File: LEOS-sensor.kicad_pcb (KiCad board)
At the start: 2 copper layers, 100 x 100 mm, 25 parts, among them J1 MicroFit_1x4, J2 MicroFit_1x4, J3 Conn_01x04_Pin, J4 Conn_01x06_Pin, J5 Conn_01x06_Pin, J6 Conn_01x05_Pin, J7 Conn_01x05_Pin, J8 Conn_01x04_Pin, U1 MCP2562FD, U2 MCP2518FD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

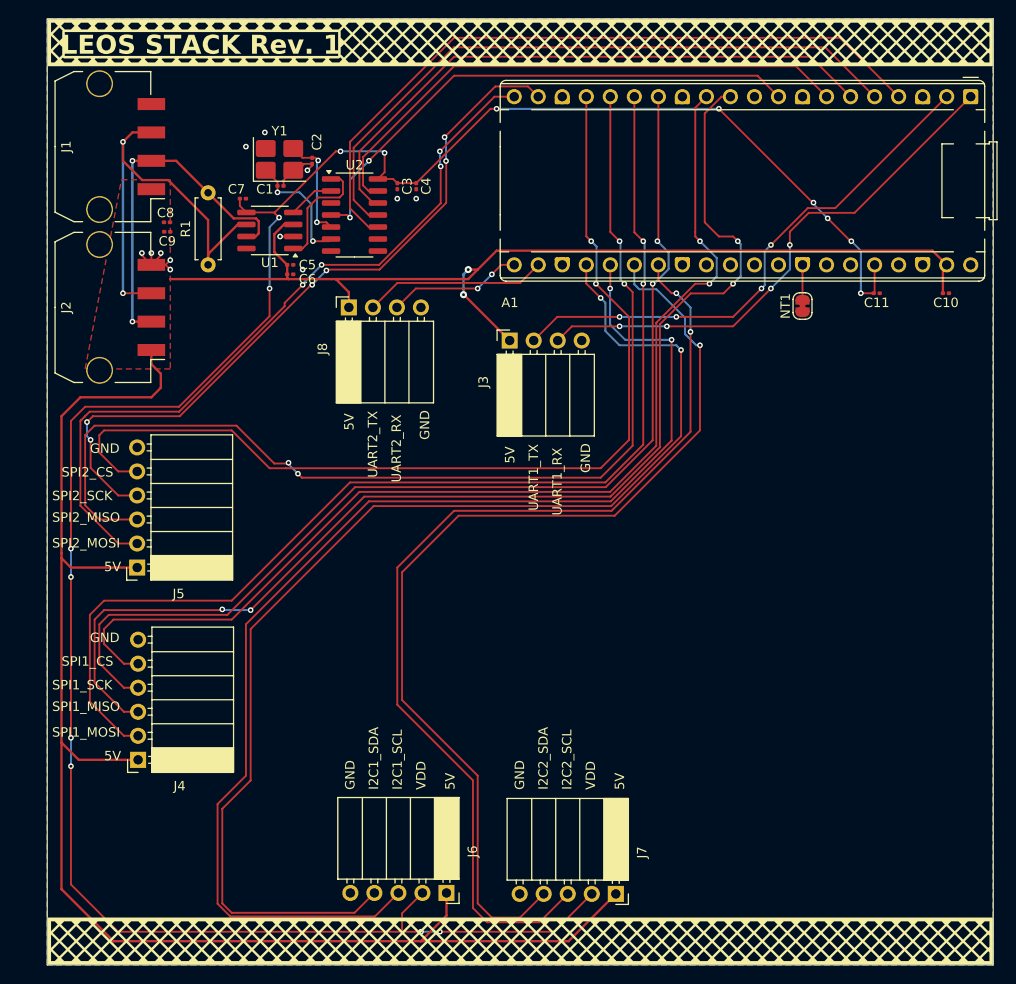
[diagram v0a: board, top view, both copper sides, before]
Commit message: Converted schematic to Socket schematics and routed all headers
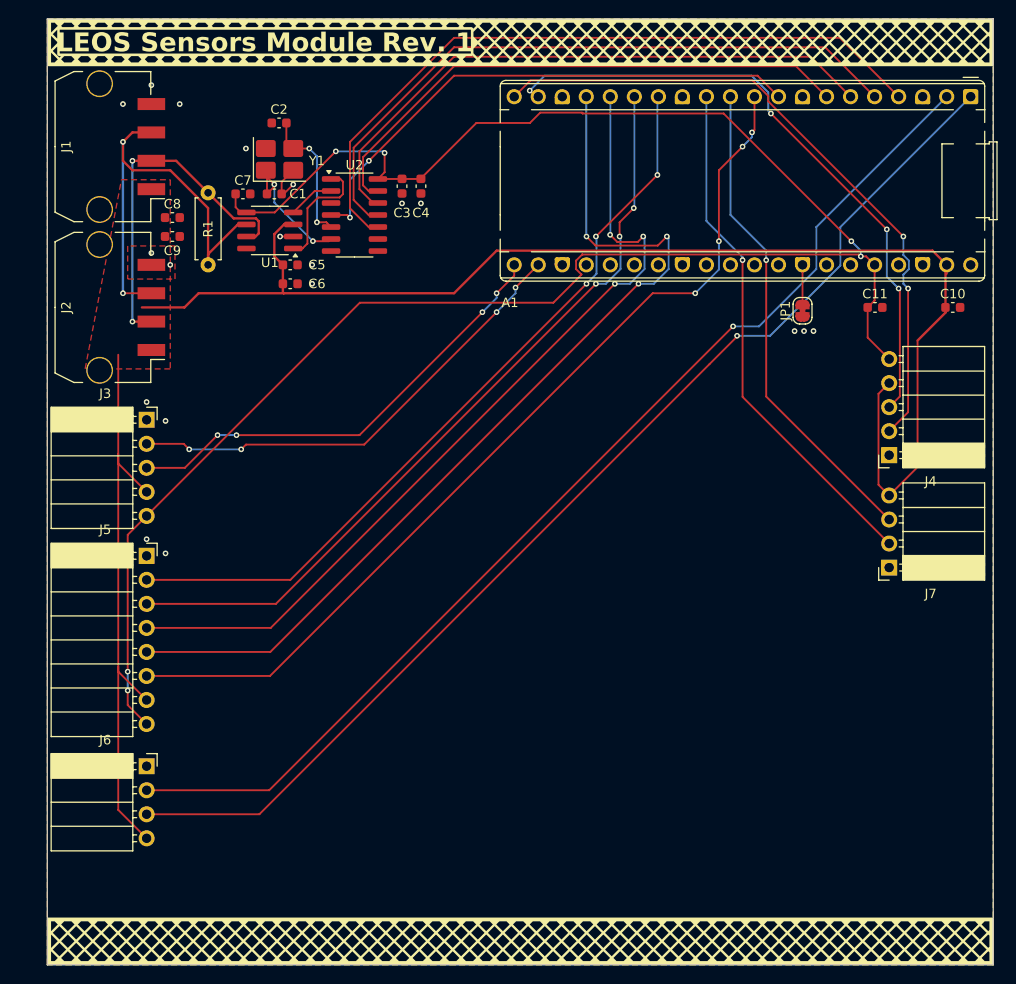
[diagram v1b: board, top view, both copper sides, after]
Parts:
- removed J8: Conn_01x04_Pin, Connector_PinSocket_2.54mm:PinSocket_1x04_P2.54mm_Horizontal
- removed NT1: NetTie_2, Jumper:SolderJumper-2_P1.3mm_Bridged_RoundedPad1.0x1.5mm
- added JP1: AGND Tie, Jumper:SolderJumper-2_P1.3mm_Bridged_RoundedPad1.0x1.5mm, F.Cu at (179.8, 80.8)
- C1, C10, C11, C2, C3, C4, C5, C6, C7, C8, C9: footprint Capacitor_SMD:C_0201_0603Metric -> Capacitor_SMD:C_0603_1608Metric
- J3: value Conn_01x04_Pin -> I2C 0; footprint Connector_PinSocket_2.54mm:PinSocket_1x04_P2.54mm_Horizontal -> Connector_PinSocket_2.54mm:PinSocket_1x05_P2.54mm_Horizontal
- J4: value Conn_01x06_Pin -> I2C 1; footprint Connector_PinSocket_2.54mm:PinSocket_1x06_P2.54mm_Horizontal -> Connector_PinSocket_2.54mm:PinSocket_1x05_P2.54mm_Horizontal
- J5: value Conn_01x06_Pin -> SPI 1; footprint Connector_PinSocket_2.54mm:PinSocket_1x06_P2.54mm_Horizontal -> Connector_PinSocket_2.54mm:PinSocket_1x08_P2.54mm_Horizontal
- J6: value Conn_01x05_Pin -> UART 0; footprint Connector_PinSocket_2.54mm:PinSocket_1x05_P2.54mm_Horizontal -> Connector_PinSocket_2.54mm:PinSocket_1x04_P2.54mm_Horizontal
- J7: value Conn_01x05_Pin -> UART 1; footprint Connector_PinSocket_2.54mm:PinSocket_1x05_P2.54mm_Horizontal -> Connector_PinSocket_2.54mm:PinSocket_1x04_P2.54mm_Horizontal
- moved J4 85.7 mm to (189.0, 96.1)
- moved J7 45.0 mm to (189.0, 108.0), turned to 180 degrees
- moved J3 39.3 mm to (110.5, 92.4), turned to 0 degrees
- moved J6 34.4 mm to (110.5, 129.0), turned to 0 degrees
- moved C2 5.32 mm to (124.5, 61.0), turned to 0 degrees
- moved C10 1.67 mm to (195.7, 80.5)
- moved J5 1.59 mm to (110.5, 106.8), turned to 0 degrees
- moved C11 1.51 mm to (187.5, 80.5)
- moved C1 1.07 mm to (124.0, 68.5)
- moved C6 1.00 mm to (125.7, 78.0)
- moved C8 0.76 mm to (113.2, 71.0)
- moved C9 0.74 mm to (113.2, 73.0)
- moved C3 0.50 mm to (137.5, 67.7)
- moved C4 0.50 mm to (139.5, 67.7)
- moved C7 0.50 mm to (120.7, 68.5)
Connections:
- A1 pad 1: UART1_RX -> UART0_TX
- A1 pad 11: SPI1_MISO -> UART1_TX
- A1 pad 12: SPI1_CS -> UART1_RX
- A1 pad 16: SPI2_MISO -> SPI1_MISO
- A1 pad 17: SPI2_CS -> SPI1_CS
- A1 pad 19: SPI2_SCK -> I2C1_SDA
- A1 pad 2: UART1_TX -> UART0_RX
- A1 pad 20: SPI2_MOSI -> I2C1_SCL
- A1 pad 21: UART2_RX -> I2C0_SDA
- A1 pad 22: UART2_TX -> I2C0_SCL
- A1 pad 24: I2C1_SDA -> GP18
- A1 pad 25: I2C1_SCL -> GP19
- A1 pad 26: I2C2_SDA -> GP20
- A1 pad 27: I2C2_SCL -> GP21
- J3 pad 1: +5V -> GND
- J3 pad 2: UART1_TX -> I2C0_SCL
- J3 pad 3: UART1_RX -> I2C0_SDA
- J3 pad 4: GND -> +5V
- J4 pad 1: +5V -> GND
- J4 pad 2: SPI1_MOSI -> I2C1_SCL
- J4 pad 3: SPI1_MISO -> I2C1_SDA
- J4 pad 4: SPI1_SCK -> +5V
- J4 pad 5: SPI1_CS -> VDD
- J5 pad 1: +5V -> GND
- J5 pad 2: SPI2_MOSI -> SPI1_SCK
- J5 pad 3: SPI2_MISO -> SPI1_MOSI
- J5 pad 4: SPI2_SCK -> SPI1_MISO
- J5 pad 5: SPI2_CS -> SPI1_CS
- J5 pad 6: GND -> GP7
- J6 pad 1: +5V -> GND
- J6 pad 2: VDD -> UART0_RX
- J6 pad 3: I2C1_SCL -> UART0_TX
- J6 pad 4: I2C1_SDA -> +5V
- J7 pad 1: +5V -> GND
- J7 pad 2: VDD -> UART1_RX
- J7 pad 3: I2C2_SCL -> UART1_TX
- J7 pad 4: I2C2_SDA -> +5V
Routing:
- net UART0_TX: track 0.00 -> 121.0 mm, vias 0 -> 1
- net UART0_RX: track 0.00 -> 117.6 mm, vias 0 -> 1
- net SPI2_MISO: track 113.1 -> 0.00 mm, vias 4 -> 0
- net I2C2_SCL: track 107.5 -> 0.00 mm, vias 2 -> 0
- net I2C2_SDA: track 106.3 -> 0.00 mm, vias 1 -> 0
- net SPI2_CS: track 103.5 -> 0.00 mm, vias 2 -> 0
- net GP7: track 0.00 -> 98.1 mm, vias 0 -> 4
- net SPI2_MOSI: track 79.8 -> 0.00 mm, vias 4 -> 0
- net SPI2_SCK: track 77.8 -> 0.00 mm, vias 6 -> 0
- net +5V: track 261.3 -> 200.3 mm, vias 2 -> 0
- net I2C1_SDA: track 127.3 -> 67.3 mm, vias 2 -> 4
- net I2C1_SCL: track 128.7 -> 71.1 mm
- net I2C0_SCL: track 0.00 -> 50.1 mm, vias 0 -> 4
- net I2C0_SDA: track 0.00 -> 48.7 mm, vias 0 -> 4
- net SPI1_MISO: track 126.7 -> 90.5 mm, vias 4 -> 3
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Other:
- board text added: "LEOS Sensors Module Rev. 1"
- board text removed: "5V"
- board text removed: "GND"
- board text removed: "I2C1_SCL"
- board text removed: "I2C1_SDA"
- board text removed: "I2C2_SCL"
- board text removed: "I2C2_SDA"
- board text removed: "LEOS STACK Rev. 1"
- board text removed: "SPI1_CS"
- board text removed: "SPI1_MISO"
- board text removed: "SPI1_MOSI"
- board text removed: "SPI1_SCK"
- board text removed: "SPI2_CS"
- board text removed: "SPI2_MISO"
- board text removed: "SPI2_MOSI"
- board text removed: "SPI2_SCK"
- board text removed: "UART1_RX"
- board text removed: "UART1_TX"
- board text removed: "UART2_RX"
- board text removed: "UART2_TX"
- board text removed: "VDD"

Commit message: added labels to pin connectors on pcb
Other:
- board text added: "5V"
- board text added: "CS1"
- board text added: "CS2"
- board text added: "GND"
- board text added: "I2C0"
- board text added: "I2C1"
- board text added: "MISO"
- board text added: "MOSI"
- board text added: "RX"
- board text added: "SCK"
- board text added: "SCL"
- board text added: "SDA"
- board text added: "SPI"
- board text added: "TX"
- board text added: "UART0"
- board text added: "UART1"
- board text added: "VDD"
